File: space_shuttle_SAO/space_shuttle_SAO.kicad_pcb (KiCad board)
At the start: 2 copper layers, 80 x 49.8 mm, 7 parts, among them J1 SAO_1.69, SW1 SW_SPDT

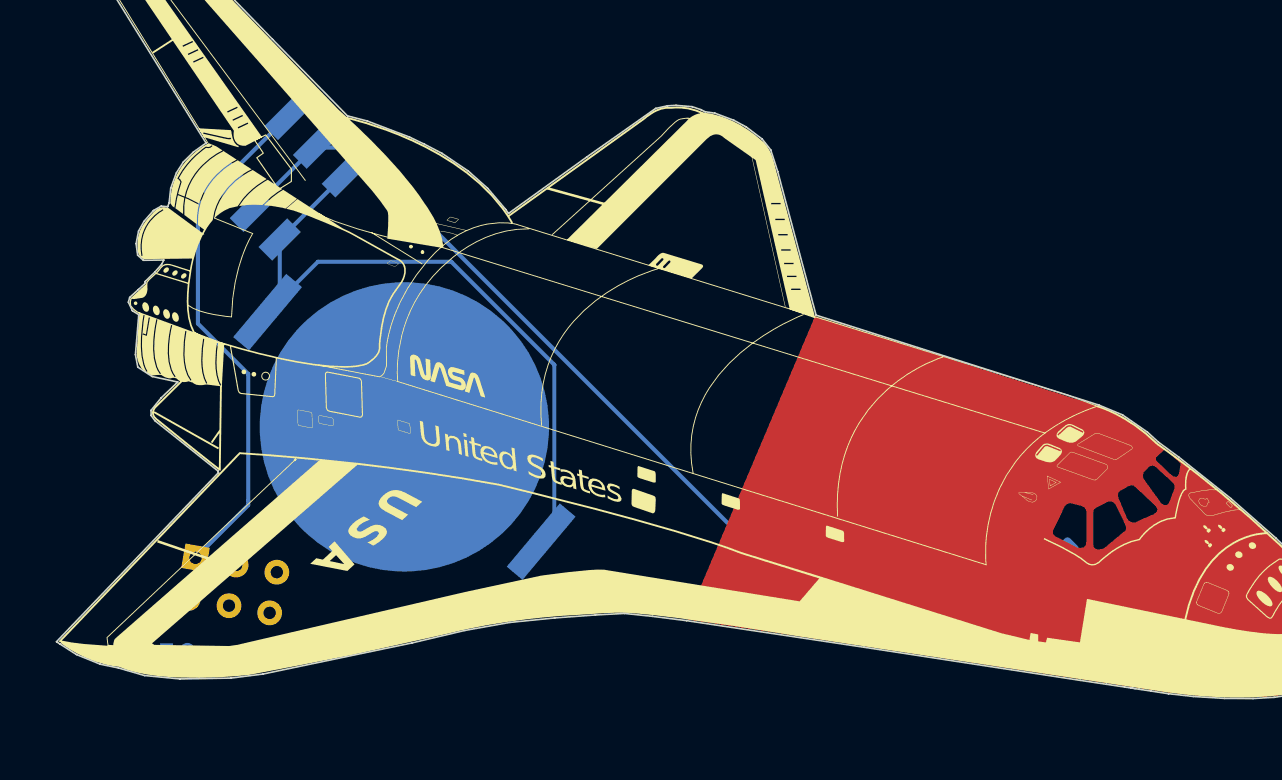
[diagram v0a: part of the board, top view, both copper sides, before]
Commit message: shuttle updates for better layout and fabrication ease.
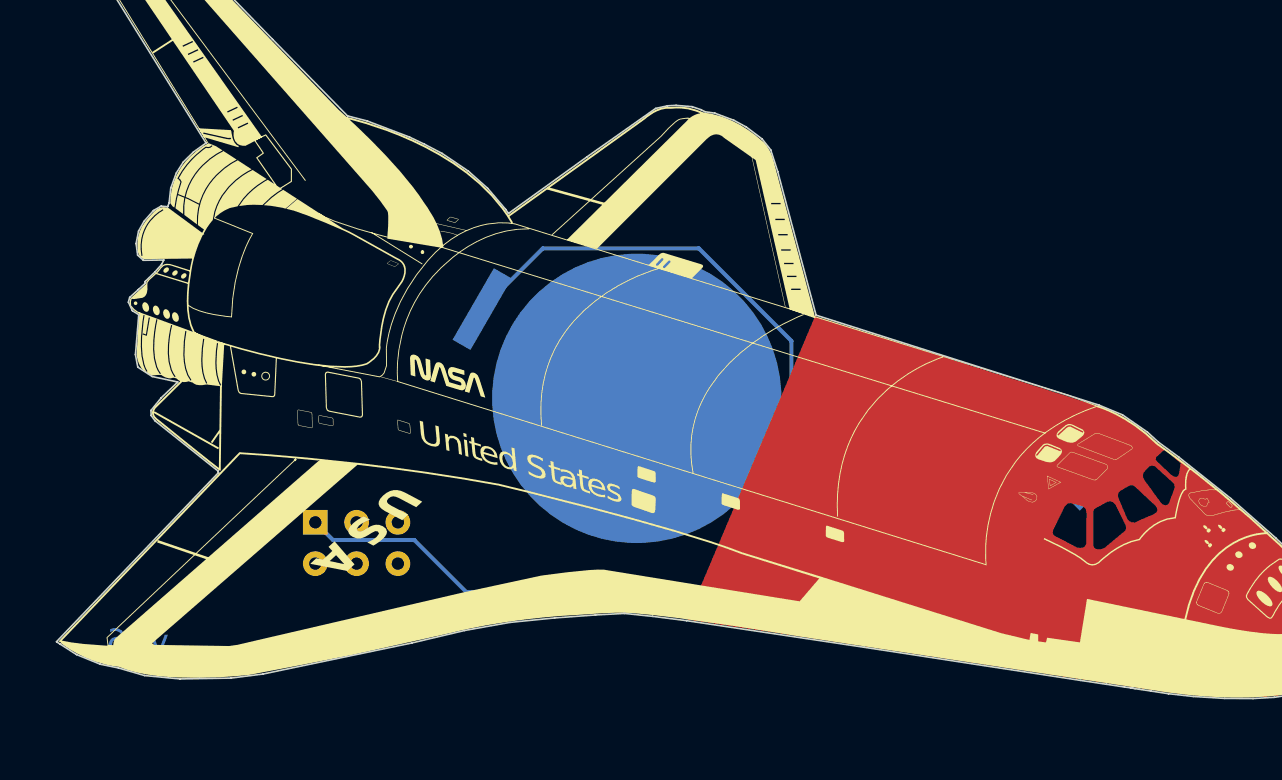
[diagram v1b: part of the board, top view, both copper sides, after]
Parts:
- moved SW1 45.3 mm to (155.6, 105.4), turned to -45 degrees
- moved svg2mod 25.5 mm to (114.4, 94.6)
- moved BT1 14.4 mm to (136.2, 99.8), turned to -30 degrees
- moved J1 12.2 mm to (119.0, 108.7), turned to 0 degrees
- moved R1 1.13 mm to (162.4, 110.6)
- moved D1 1.02 mm to (165.7, 107.2)
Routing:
- net Net-(R1-Pad1): track 61.9 -> 14.5 mm
- net Net-(J1-Pad1): track 31.9 -> 47.3 mm
- net Net-(BT1-Pad1): track 43.0 -> 43.7 mm
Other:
- board text added: "v06"
- board text removed: "SAO V.1.69"
- board text removed: "v05"

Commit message: fixes to v01 schematic
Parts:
- moved R1 9.20 mm to (171.6, 111.5), turned to 45 degrees
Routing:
- net Net-(R1-Pad1): track 14.5 -> 26.3 mm
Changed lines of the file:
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@@
   )
   (footprint "Resistors_SMD:R_1206_3216Metric" (layer "B.Cu")
-    (at 162.432466 110.612094 -45)
+    (at 171.587738 111.474689 45)
     (descr "Resistor SMD 1206 (3216 Metric), square (rectangular) end terminal, IPC_7351 nominal, (Body size source: IPC-SM-782 page 72, https://www.pcb-3d.com/wordpress/wp-content/uploads/ipc-sm-782a_amendment_1_and_2.pdf), generated with kicad-footprint-generator")
     (tags "resistor")
@@
     (property "Sheetname" "")
     (attr smd)
-    (fp_text reference "R1" (at 0 1.82 -45) (layer "B.SilkS") hide
-      (effects (font (size 1 1) (thickness 0.15)) (justify mirror))
-    )
-    (fp_text value "330" (at 0 -1.82 -45) (layer "B.Fab")
-      (effects (font (size 1 1) (thickness 0.15)) (justify mirror))
-    )
-    (fp_text user "${REFERENCE}" (at 0 0 -45) (layer "B.Fab")
+    (fp_text reference "R1" (at 0 1.82 45) (layer "B.SilkS") hide
+      (effects (font (size 1 1) (thickness 0.15)) (justify mirror))
+    )
+    (fp_text value "330" (at 0 -1.82 45) (layer "B.Fab")
+      (effects (font (size 1 1) (thickness 0.15)) (justify mirror))
+    )
+    (fp_text user "${REFERENCE}" (at 0 0 45) (layer "B.Fab")
       (effects (font (size 0.8 0.8) (thickness 0.12)) (justify mirror))
     )
@@
     (fp_line (start -1.6 -0.8) (end -1.6 0.8) (layer "B.Fab") (width 0.1))
     (fp_line (start 1.6 -0.8) (end -1.6 -0.8) (layer "B.Fab") (width 0.1))
-    (pad "1" smd roundrect locked (at -1.4625 0 315) (size 1.125 1.75) (layers "B.Cu" "B.Paste" "B.Mask") (roundrect_rratio 0.2222204444)
+    (pad "1" smd roundrect locked (at -1.4625 0 45) (size 1.125 1.75) (layers "B.Cu" "B.Paste" "B.Mask") (roundrect_rratio 0.2222204444)
       (net 9 "Net-(R1-Pad1)") (pintype "passive"))
-    (pad "2" smd roundrect locked (at 1.4625 0 315) (size 1.125 1.75) (layers "B.Cu" "B.Paste" "B.Mask") (roundrect_rratio 0.2222204444)
+    (pad "2" smd roundrect locked (at 1.4625 0 45) (size 1.125 1.75) (layers "B.Cu" "B.Paste" "B.Mask") (roundrect_rratio 0.2222204444)
       (net 1 "Net-(D1-Pad2)") (pintype "passive"))
     (model "${KISYS3DMOD}/Resistor_SMD.3dshapes/R_1206_3216Metric.wrl"
@@
       (effects (font (size 1 1) (thickness 0.15)) (justify mirror))
     )
-    (fp_text user "SAO PWR" (at 4.351288 0.072123 45) (layer "B.SilkS")
+    (fp_text user "SAO PWR" (at 5.420138 0.092276 45) (layer "B.SilkS")
       (effects (font (size 0.7 0.7) (thickness 0.15)) (justify mirror))
     )
-    (fp_text user "Battery PWR" (at -4.694706 -0.161155 45) (layer "B.SilkS")
+    (fp_text user "Battery PWR" (at -5.766354 0.047351 45) (layer "B.SilkS")
       (effects (font (size 0.7 0.7) (thickness 0.15)) (justify mirror))
     )
@@
     (effects (font (size 2 2) (thickness 0.4)) (justify mirror))
   )
-  (segment (start 163.46661 111.646238) (end 164.953184 111.646238) (width 0.25) (layer "B.Cu") (net 1))
-  (segment (start 164.953184 111.646238) (end 167.574855 109.024567) (width 0.25) (layer "B.Cu") (net 1))
+  (segment (start 172.621882 110.440545) (end 171.205904 109.024567) (width 0.25) (layer "B.Cu") (net 1))
+  (segment (start 171.205904 109.024567) (end 167.574855 109.024567) (width 0.25) (layer "B.Cu") (net 1))
   (segment (start 159.300591 105.208202) (end 155.411503 109.09729) (width 0.25) (layer "B.Cu") (net 3))
   (segment (start 117.527956 108.560398) (end 122.530398 108.560398) (width 0.25) (layer "B.Cu") (net 3))
@@
   (segment (start 145.731338 105.339334) (end 151.653547 105.339334) (width 0.25) (layer "B.Cu") (net 8))
   (segment (start 145.731338 96.314002) (end 145.731338 105.339334) (width 0.25) (layer "B.Cu") (net 8))
-  (segment (start 161.398322 109.57795) (end 161.398322 105.078547) (width 0.25) (layer "B.Cu") (net 9))
-  (segment (start 161.398322 105.078547) (end 159.76021 103.440435) (width 0.25) (layer "B.Cu") (net 9))
+  (segment (start 159.76021 103.440435) (end 161.29 104.970225) (width 0.25) (layer "B.Cu") (net 9))
+  (segment (start 161.29 111.76) (end 162.038833 112.508833) (width 0.25) (layer "B.Cu") (net 9))
+  (segment (start 162.038833 112.508833) (end 170.553594 112.508833) (width 0.25) (layer "B.Cu") (net 9))
   (segment (start 153.643736 107.329523) (end 157.532824 103.440435) (width 0.25) (layer "B.Cu") (net 9))
-  (segment (start 159.76021 103.440435) (end 157.532824 103.440435) (width 0.25) (layer "B.Cu") (net 9))
+  (segment (start 157.532824 103.440435) (end 159.76021 103.440435) (width 0.25) (layer "B.Cu") (net 9))
+  (segment (start 161.29 104.970225) (end 161.29 111.76) (width 0.25) (layer "B.Cu") (net 9))
   (zone (net 2) (net_name "GND") (layer "F.Cu") (hatch edge 0.508)
     (connect_pads (clearance 0.508))

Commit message: adjusted b.cu keepout zone and removed jlc text for macrofab
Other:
- board text removed: "JLCJLCJLCJLC"
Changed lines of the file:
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@@
     (effects (font (size 1.5 1.5) (thickness 0.3)) (justify mirror))
-  )
-  (gr_text "JLCJLCJLCJLC" (at 130.7718 108.369082 -30) (layer "B.SilkS")
-    (effects (font (size 0.9 0.9) (thickness 0.15)) (justify mirror))
   )
   (gr_text "@cybertestpilot" (at 107.516966 75.840706 -55) (layer "B.SilkS")
@@
     (polygon
       (pts
-        (xy 167.6654 105.42016)
-        (xy 168.28008 106.13644)
-        (xy 168.25468 106.92384)
-        (xy 167.90924 107.59948)
-        (xy 167.30472 108.03128)
-        (xy 166.40048 108.14304)
-        (xy 165.61308 107.6706)
-        (xy 165.19652 106.68)
-        (xy 165.44036 105.83672)
-        (xy 165.87216 105.37952)
-        (xy 166.61892 105.1052)
+        (xy 166.723714 105.836291)
+        (xy 167.338394 106.552571)
+        (xy 167.312994 107.339971)
+        (xy 166.967554 108.015611)
+        (xy 166.363034 108.447411)
+        (xy 165.458794 108.559171)
+        (xy 164.671394 108.086731)
+        (xy 164.254834 107.096131)
+        (xy 164.498674 106.252851)
+        (xy 164.930474 105.795651)
+        (xy 165.677234 105.521331)
       )
     )

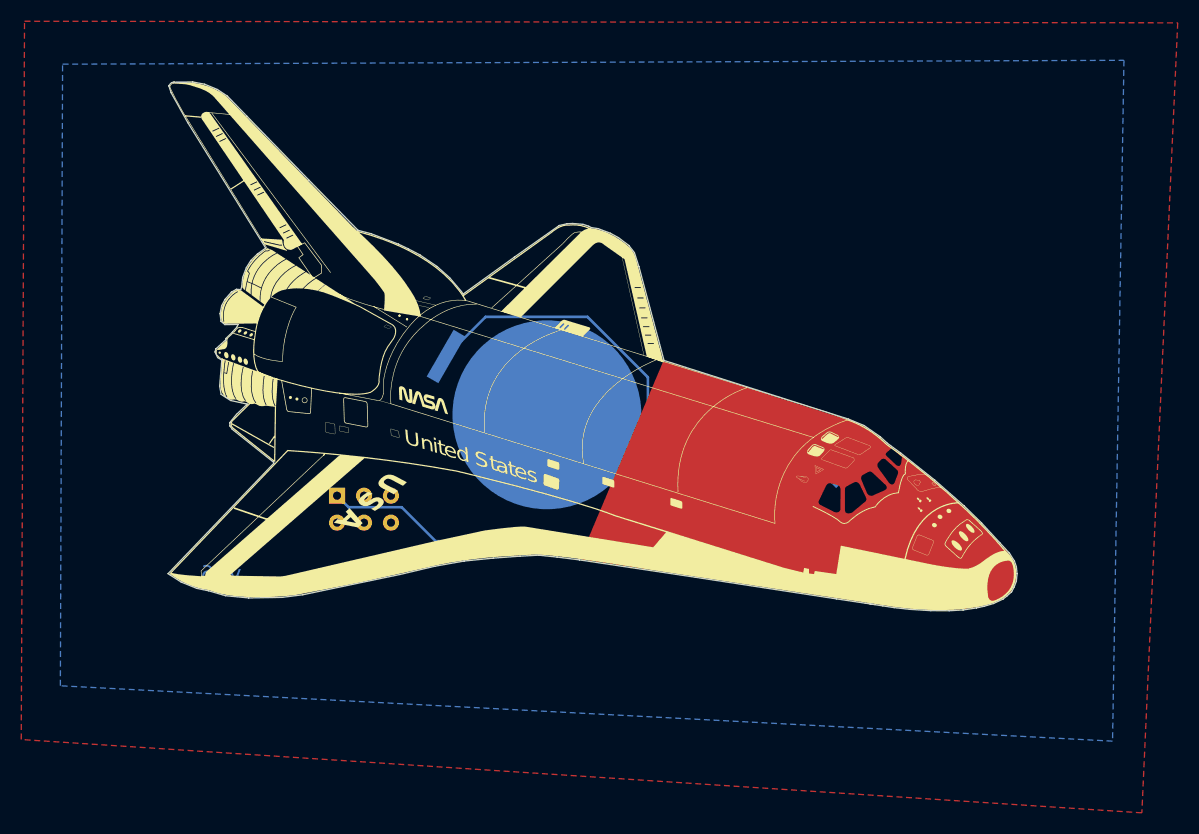
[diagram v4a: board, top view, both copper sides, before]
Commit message: increased edge cuts offset to meet minimum 0.254mm threshold.
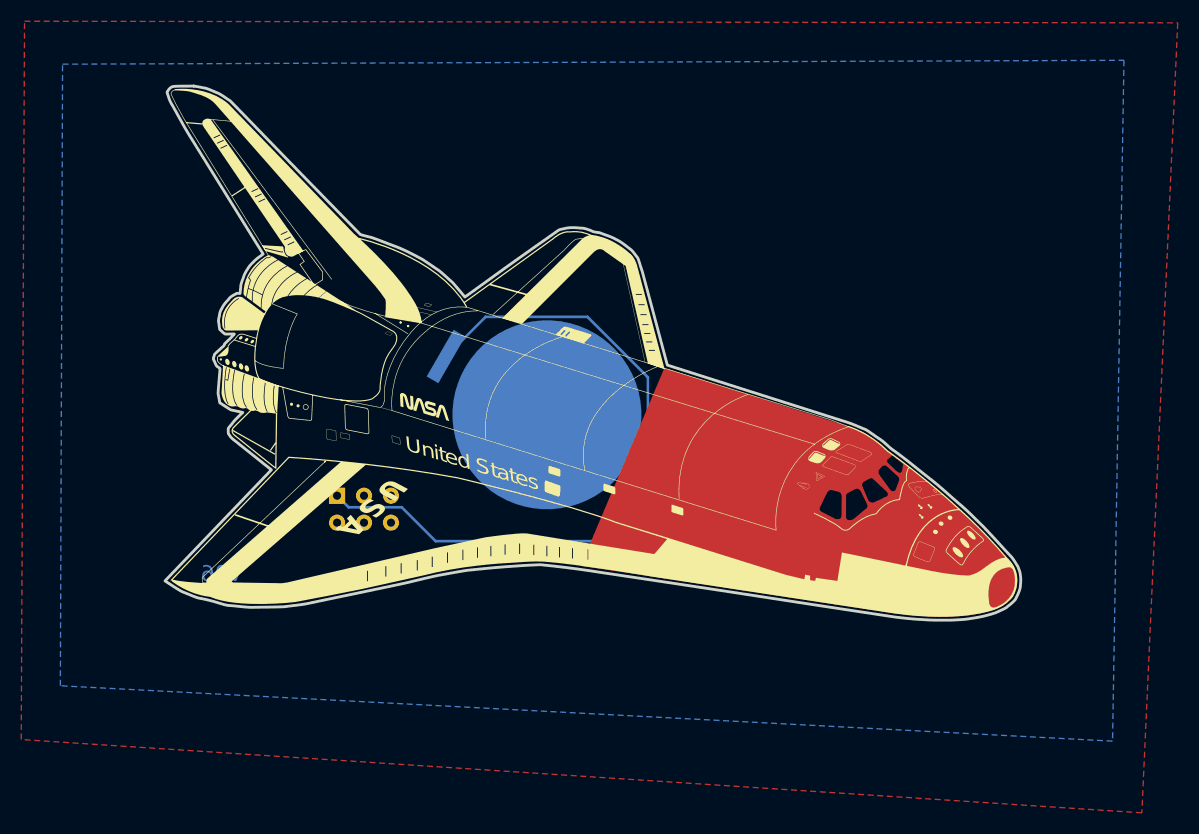
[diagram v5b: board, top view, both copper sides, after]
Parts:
- moved svg2mod 20.5 mm to (140.5, 94.0)
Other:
- board size 80 x 49.8 mm -> 80.6 x 50.3 mm
